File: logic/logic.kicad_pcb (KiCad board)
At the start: 2 copper layers, 157 x 79.4 mm, 36 parts, among them J1 DIN41612_03x32_ABC, J2 Conn_02x05_Odd_Even, J3 Conn_02x05_Odd_Even, J4 Conn_02x05_Odd_Even, U1 TPIC6595, U14 74HC14, U2 TPIC6595, U3 TPIC6595, U4 TPIC6595, U5 TPIC6595, U6 TPIC6595, U7 TPIC6595, U8 TPIC6595, U9 74HCT244

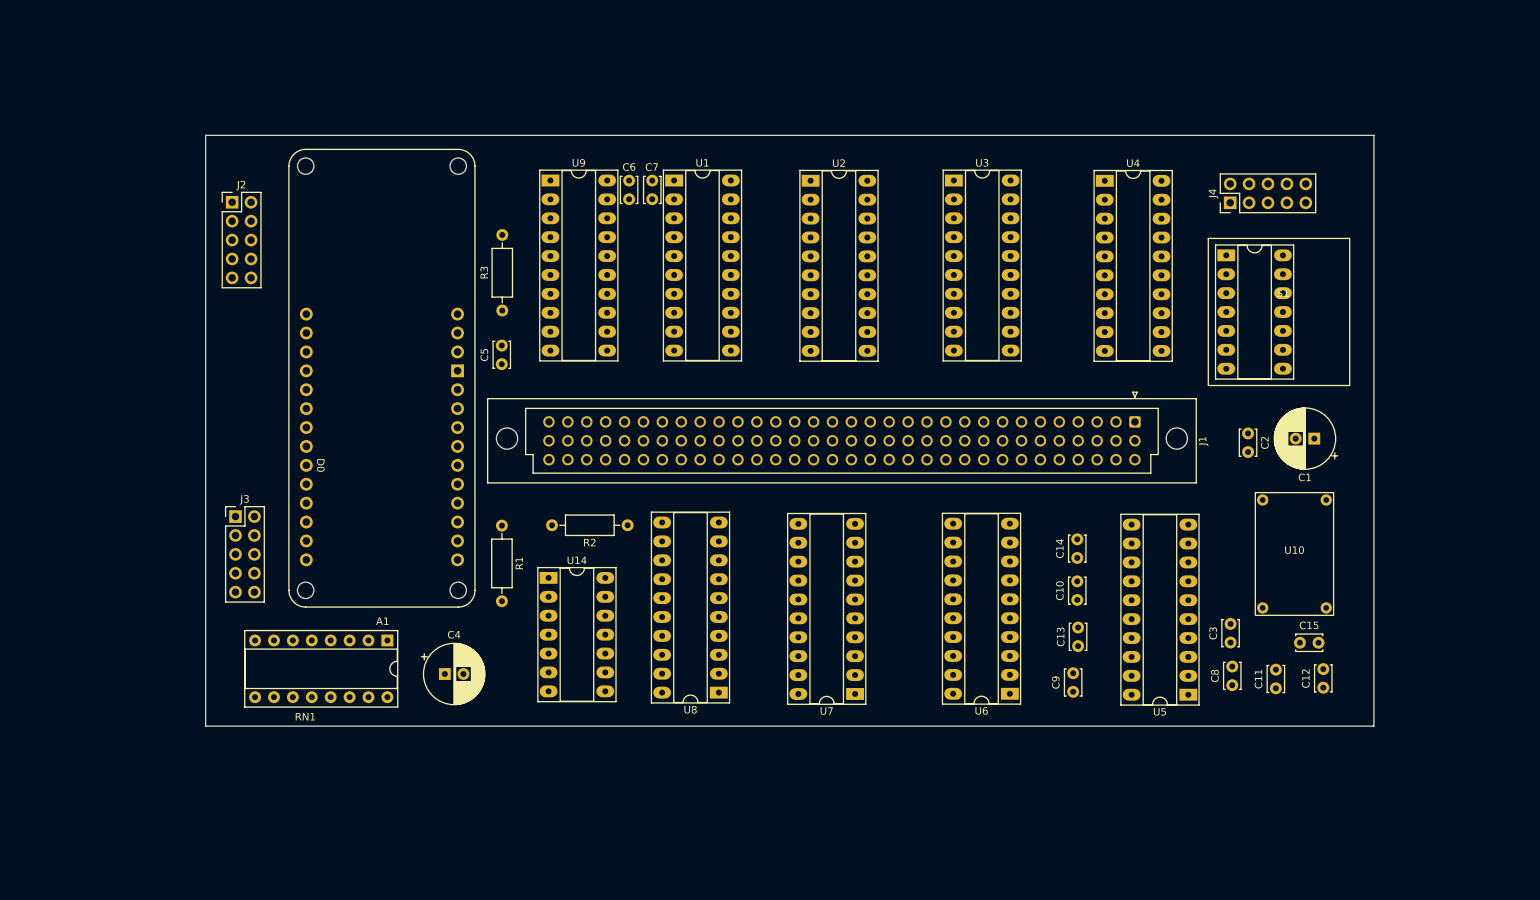
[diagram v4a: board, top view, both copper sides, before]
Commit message: Proposed final display board positioning
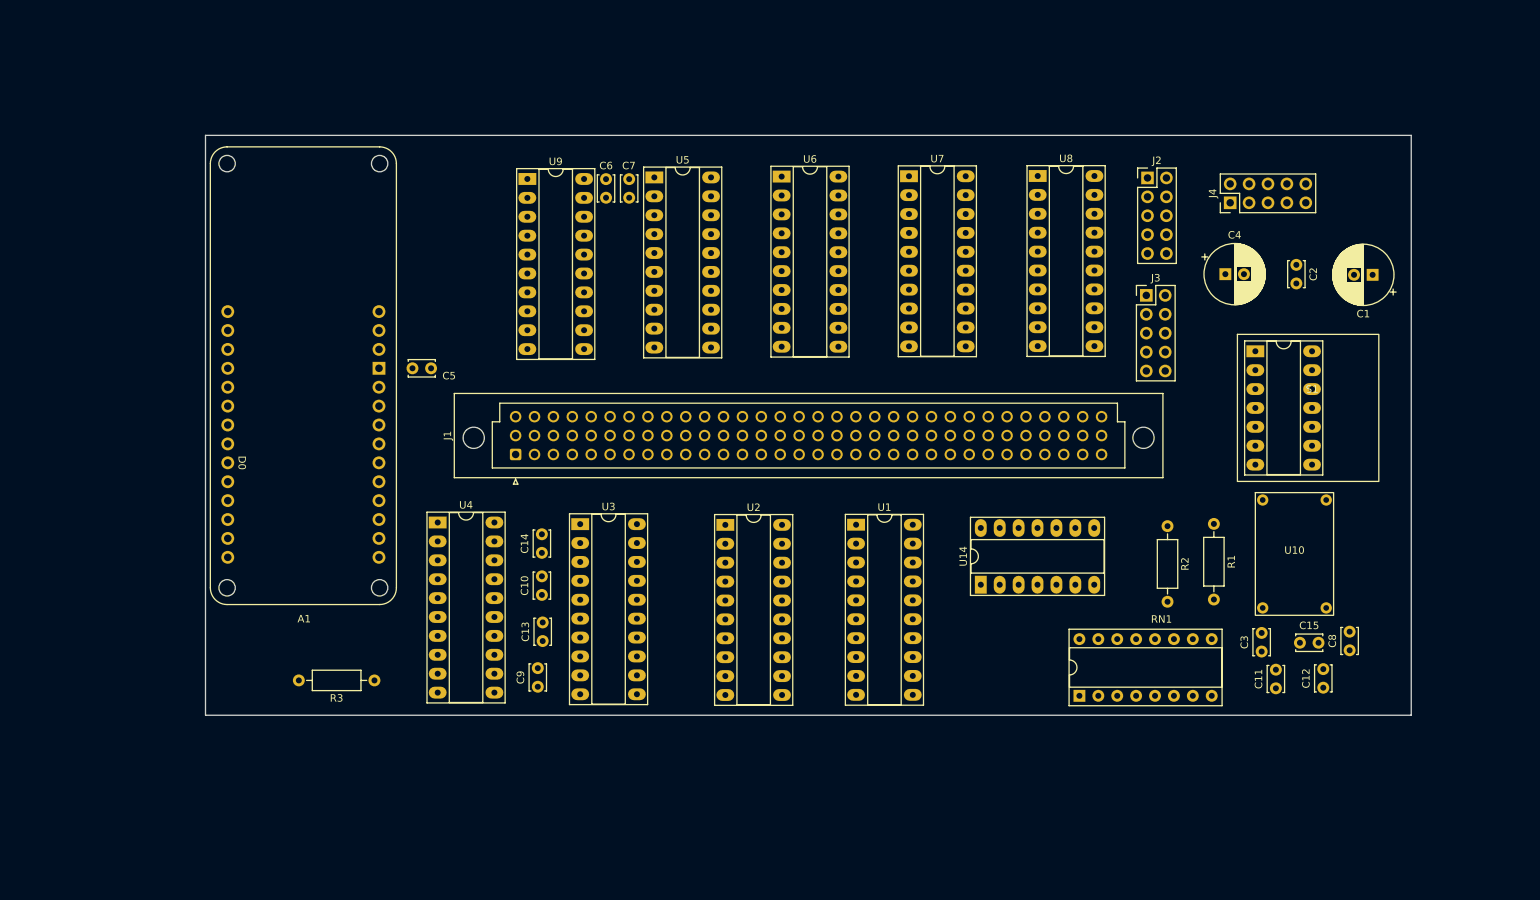
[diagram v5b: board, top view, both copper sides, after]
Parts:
- moved J3 125.9 mm to (196.5, 71.6)
- moved J2 123.0 mm to (196.7, 55.8)
- moved C4 117.8 mm to (207.1, 68.8)
- moved U4 100.7 mm to (101.3, 102.1)
- moved U5 99.9 mm to (130.4, 55.8), turned to 0 degrees
- moved R1 95.7 mm to (205.6, 102.3)
- moved RN1 93.3 mm to (187.5, 125.4), turned to 90 degrees
- moved J1 83.3 mm to (111.7, 93.0), turned to 90 degrees
- moved U8 81.6 mm to (181.9, 55.6), turned to 0 degrees
- moved U6 76.0 mm to (147.5, 55.7), turned to 0 degrees
- moved R2 72.6 mm to (199.3, 102.6), turned to -90 degrees
- moved C10 71.9 mm to (115.3, 111.9)
- moved C14 71.9 mm to (115.3, 106.2)
- moved C13 71.9 mm to (115.4, 118.1)
- moved C9 71.9 mm to (114.7, 124.2)
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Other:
- board size 157 x 79.4 mm -> 162 x 77.9 mm
- board text added: "KEEP CLEAR"

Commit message: Ongoing layout work on logic board.
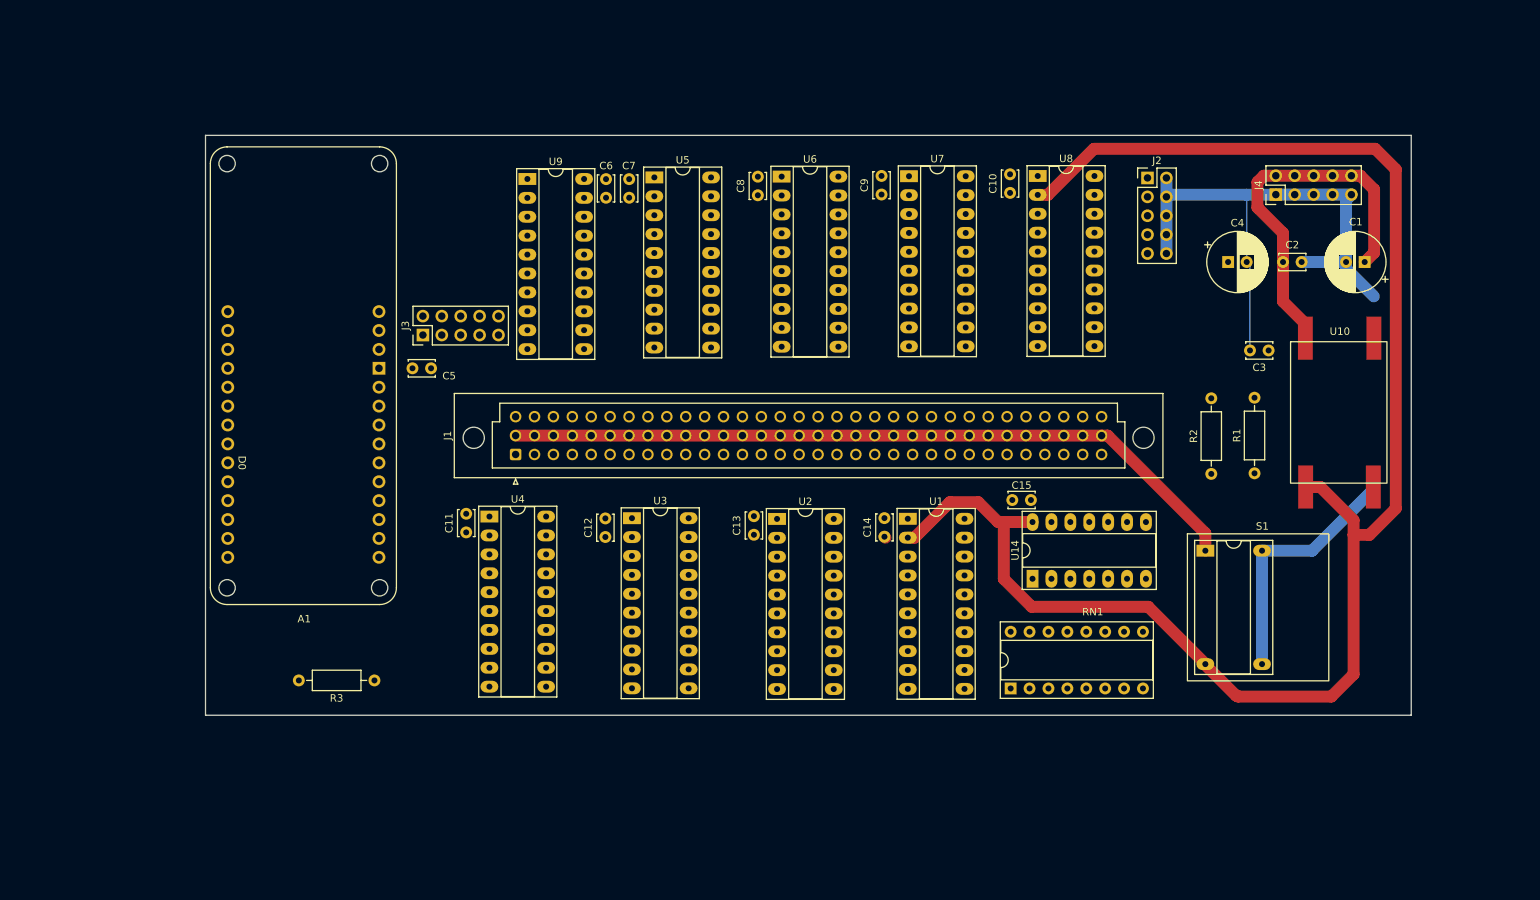
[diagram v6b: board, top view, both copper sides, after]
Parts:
- moved C11 110.8 mm to (105.1, 103.5)
- moved C8 100.3 mm to (144.3, 58.2)
- moved C12 98.6 mm to (123.8, 104.1)
- moved J3 97.4 mm to (99.3, 77.0), turned to 90 degrees
- moved C10 82.9 mm to (178.2, 57.9)
- moved C9 80.7 mm to (160.9, 58.1)
- moved C14 46.1 mm to (161.3, 104.0)
- moved C15 40.9 mm to (181.0, 99.1), turned to 180 degrees
- moved C3 40.5 mm to (212.9, 79.0), turned to 180 degrees
- moved C13 31.8 mm to (143.8, 103.8)
- moved S1 27.6 mm to (212.1, 108.5)
- moved U10 19.9 mm to (222.4, 87.4)
- moved RN1 9.29 mm to (178.3, 124.4)
- moved R2 9.16 mm to (205.2, 95.6), turned to 90 degrees
- moved R1 8.72 mm to (211.0, 95.5), turned to 90 degrees
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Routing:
- net V5.0: track 0.00 -> 219.9 mm
- net GND: track 0.00 -> 111.4 mm
- net V170: track 0.00 -> 100.5 mm
- net Net-(J4-Pin_10): track 0.00 -> 50.7 mm
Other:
- copper layers 2 -> 4
- board text removed: "KEEP CLEAR"

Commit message: Tenatively, all parts in final positions
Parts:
- moved RN1 103.9 mm to (74.4, 124.7)
- moved J2 80.0 mm to (116.7, 53.9)
- moved R3 74.2 mm to (108.6, 53.9), turned to 180 degrees
- moved C5 20.9 mm to (107.7, 101.0)
- moved C15 19.3 mm to (199.4, 104.7), turned to -90 degrees
- moved J3 15.2 mm to (114.1, 74.0), turned to -90 degrees
- moved C7 14.3 mm to (141.3, 58.5)
- moved U5 13.8 mm to (144.2, 56.0)
- moved C6 13.5 mm to (137.2, 56.2), turned to -90 degrees
- moved U9 13.3 mm to (126.6, 56.2)
- moved C8 11.9 mm to (156.2, 58.5)
- moved U6 11.7 mm to (159.1, 56.0)
- moved C9 10.3 mm to (171.2, 58.5)
- moved U7 9.58 mm to (174.2, 56.0)
- moved U14 9.18 mm to (188.9, 104.7), turned to 0 degrees
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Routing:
- net V5.0: track 219.9 -> 0.00 mm
- net GND: track 111.4 -> 0.00 mm
- net V170: track 100.5 -> 0.00 mm
- net Net-(J4-Pin_10): track 50.7 -> 0.00 mm

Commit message: Ongoing development - logic board routing
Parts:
- moved R2 29.6 mm to (197.8, 124.3), turned to 180 degrees
- moved C3 24.3 mm to (221.0, 101.9), turned to 0 degrees
- moved R1 13.3 mm to (199.4, 102.0), turned to 180 degrees
- moved C15 0.55 mm to (199.4, 105.2)
- moved U14 0.55 mm to (188.8, 105.2)
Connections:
- J1 pad b17: V170 -> GND
- J1 pad b18: V170 -> GND
- J1 pad b19: V170 -> GND
- J1 pad b20: V170 -> GND
- J1 pad b21: V170 -> GND
- J1 pad b22: V170 -> GND
- J1 pad b23: V170 -> GND
- J1 pad b24: V170 -> GND
- J1 pad b25: V170 -> GND
- J1 pad b26: V170 -> GND
- J1 pad b27: V170 -> GND
- J1 pad b28: V170 -> GND
- J1 pad b29: V170 -> GND
- J1 pad b30: V170 -> GND
- J1 pad b31: V170 -> GND
- J1 pad b32: V170 -> GND
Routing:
- net GND: track 0.00 -> 707.5 mm, vias 0 -> 18
- net V5.0: track 0.00 -> 341.0 mm, vias 0 -> 4
- net V170: track 0.00 -> 151.3 mm
- net POR: track 0.00 -> 96.2 mm
- net Net-(J4-Pin_10): track 0.00 -> 75.9 mm
- net Net-(C4-Pad1): track 0.00 -> 75.3 mm, vias 0 -> 1
- net /SRCK: track 0.00 -> 59.4 mm
- net /~{SRCLR}: track 0.00 -> 59.4 mm
- net /RCLK: track 0.00 -> 59.3 mm
- net /B1-4: track 0.00 -> 28.7 mm
- net /B1-5: track 0.00 -> 28.1 mm
- net /B1-3: track 0.00 -> 27.5 mm
- net /B1-6: track 0.00 -> 27.4 mm
- net /B1-7: track 0.00 -> 26.2 mm
- net /B1-2: track 0.00 -> 24.0 mm
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- added copper zone on B.Cu, net GND
